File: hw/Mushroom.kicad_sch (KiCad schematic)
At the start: 4 parts, among them U1 STM32G030F6Px, U2 LPS22HH, U3 SHT30-DIS, U4 BH1750FVI-TR

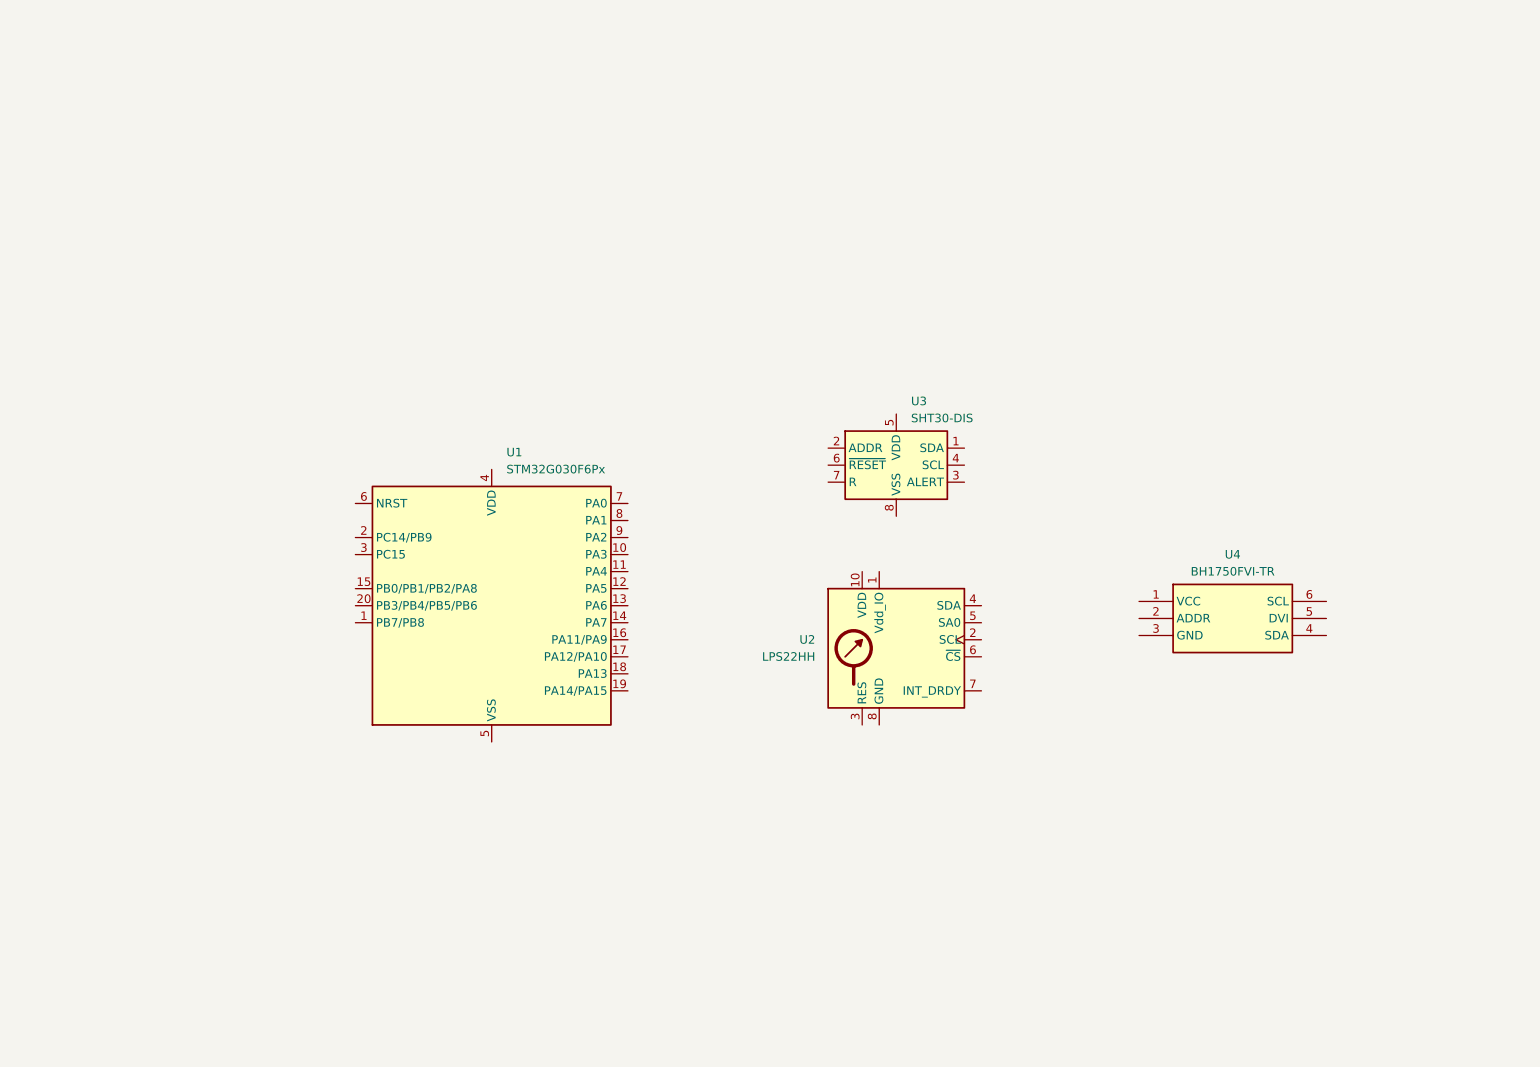
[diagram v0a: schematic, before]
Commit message: Finish schematic
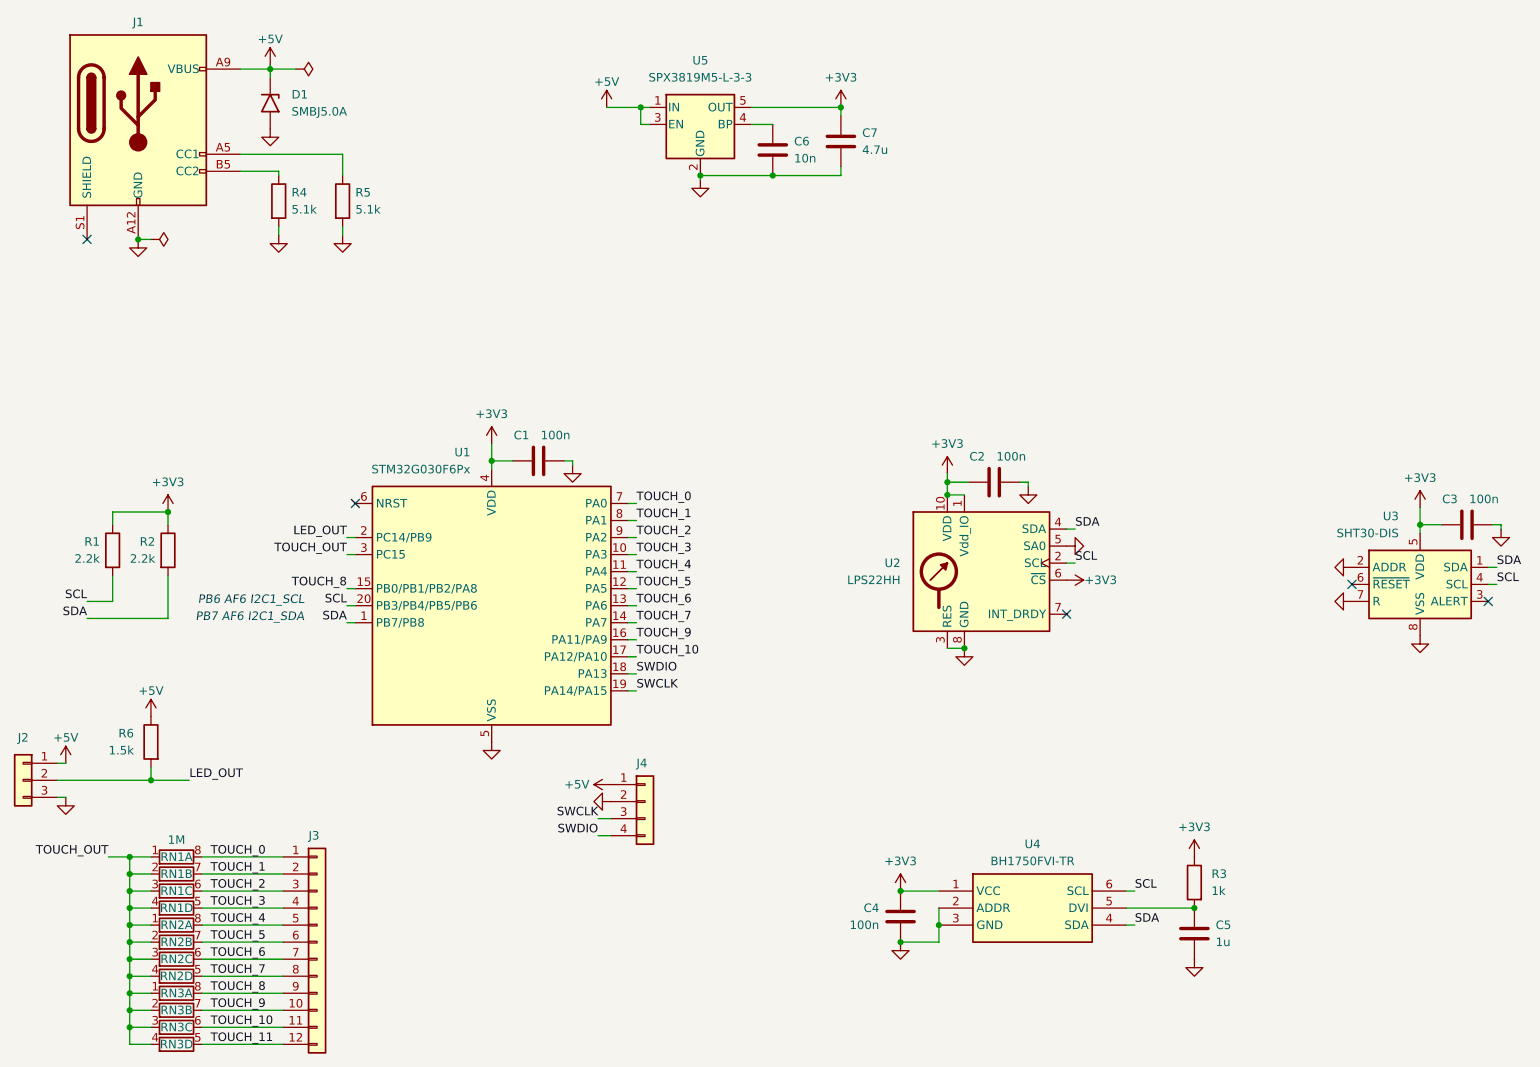
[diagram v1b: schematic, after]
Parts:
- added C1, C2, C3, C4: 100n, Capacitor_SMD:C_0402_1005Metric, symbol Device:C
- added C5: 1u, Capacitor_SMD:C_0402_1005Metric, symbol Device:C
- added C6: 10n, Capacitor_SMD:C_0402_1005Metric, symbol Device:C
- added C7: 4.7u, Capacitor_SMD:C_0402_1005Metric, symbol Device:C
- added D1: SMBJ5.0A, Diode_SMD:D_SMB, symbol Diode:SMF5V0A
- added J1: USB_C_Receptacle_PowerOnly_6P, Mushroom_footprints:USB_C_Receptacle, symbol Connector:USB_C_Receptacle_PowerOnly_6P
- added J2: Conn_01x03, Connector_PinHeader_2.54mm:PinHeader_1x03_P2.54mm_Vertical, symbol Connector_Generic:Conn_01x03
- added J3: Conn_01x12, Connector_PinHeader_2.54mm:PinHeader_2x06_P2.54mm_Vertical, symbol Connector_Generic:Conn_01x12
- added J4: Conn_01x04, Mushroom_footprints:TestPoints_1x04_P2.0, symbol Connector_Generic:Conn_01x04
- added R1, R2: 2.2k, Resistor_SMD:R_0402_1005Metric, symbol Device:R
- added R3: 1k, Resistor_SMD:R_0402_1005Metric, symbol Device:R
- added R4, R5: 5.1k, Resistor_SMD:R_0402_1005Metric, symbol Device:R
- added R6: 1.5k, Resistor_SMD:R_0402_1005Metric, symbol Device:R
- added RN1, RN2, RN3: 1M, Resistor_SMD:R_Array_Convex_4x0402, symbol Mushroom_symbols:R_Network04_Split
- added U5: SPX3819M5-L-3-3, Package_TO_SOT_SMD:SOT-23-5, symbol Regulator_Linear:SPX3819M5-L-3-3
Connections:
- net SDA: now reaches U3.1 (SDA)
- net SDA: now also U1.1 (PB7/PB8), U2.4 (SDA), U4.4 (SDA), R2.2
- net GND: now reaches U3.2 (ADDR)
- net GND: now also U1.5 (VSS), U2.3 (RES), U2.5 (SA0), U2.8 (GND), U2.9 (GND), U3.7 (R), U3.8 (VSS), U3.9 (VSS), U4.2 (ADDR), U4.3 (GND), C1.2, C2.2, C3.2, C4.2, C5.2, C6.2, C7.2, D1.2 (A2), J1.A12 (GND), J1.B12 (GND), J2.3 (Pin_3), J4.2 (Pin_2), R4.2, R5.2, U5.2 (GND)
- net SCL: now reaches U3.4 (SCL)
- net SCL: now also U1.20 (PB3/PB4/PB5/PB6), U2.2 (SCL), U4.6 (SCL), R1.2
- net +3V3: now reaches U3.5 (VDD)
- net +3V3: now also U1.4 (VDD), U2.1 (Vdd_IO), U2.10 (VDD), U2.6 (~{CS}), U4.1 (VCC), C1.1, C2.1, C3.1, C4.1, C7.1, R1.1, R2.1, R3.1, U5.5 (OUT)
- net TOUCH_3: now reaches U1.10 (PA3)
- net TOUCH_3: now also J3.4 (Pin_4), RN1.5 (R4.2)
- net TOUCH_4: now reaches U1.11 (PA4)
- net TOUCH_4: now also J3.5 (Pin_5), RN2.8 (R1.2)
- net TOUCH_5: now reaches U1.12 (PA5)
- net TOUCH_5: now also J3.6 (Pin_6), RN2.7 (R2.2)
- net TOUCH_6: now reaches U1.13 (PA6)
- net TOUCH_6: now also J3.7 (Pin_7), RN2.6 (R3.2)
- net TOUCH_7: now reaches U1.14 (PA7)
- net TOUCH_7: now also J3.8 (Pin_8), RN2.5 (R4.2)
- net TOUCH_8: now reaches U1.15 (PB0/PB1/PB2/PA8)
- net TOUCH_8: now also J3.9 (Pin_9), RN3.8 (R1.2)
- net TOUCH_9: now reaches U1.16 (PA11/PA9)
- net TOUCH_9: now also J3.10 (Pin_10), RN3.7 (R2.2)
- net TOUCH_10: now reaches U1.17 (PA12/PA10)
- net TOUCH_10: now also J3.11 (Pin_11), RN3.6 (R3.2)
- net SWDIO: now reaches U1.18 (PA13)
- net SWDIO: now also J4.4 (Pin_4)
- net SWCLK: now reaches U1.19 (PA14/PA15)
- net SWCLK: now also J4.3 (Pin_3)
- net LED_OUT: now reaches U1.2 (PC14/PB9)
- net LED_OUT: now also J2.2 (Pin_2), R6.2
- net TOUCH_OUT: now reaches U1.3 (PC15)
- net TOUCH_OUT: now also RN1.1 (R1.1), RN1.2 (R2.1), RN1.3 (R3.1), RN1.4 (R4.1), RN2.1 (R1.1), RN2.2 (R2.1), RN2.3 (R3.1), RN2.4 (R4.1), RN3.1 (R1.1), RN3.2 (R2.1), RN3.3 (R3.1), RN3.4 (R4.1)
- net TOUCH_0: now reaches U1.7 (PA0)
- net TOUCH_0: now also J3.1 (Pin_1), RN1.8 (R1.2)
- net TOUCH_1: now reaches U1.8 (PA1)
- net TOUCH_1: now also J3.2 (Pin_2), RN1.7 (R2.2)
- net TOUCH_2: now reaches U1.9 (PA2)
- net TOUCH_2: now also J3.3 (Pin_3), RN1.6 (R3.2)
- net at U4.5 (DVI): now also C5.1, R3.2
- new net: C6.1, U5.4 (BP)
- new net: J1.A5 (CC1), R5.1
- new net: J1.B5 (CC2), R4.1
- new net +5V: D1.1 (A1), J1.A9 (VBUS), J1.B9 (VBUS), J2.1 (Pin_1), J4.1 (Pin_1), R6.1, U5.1 (IN), U5.3 (EN)
- new net TOUCH_11: J3.12 (Pin_12), RN3.5 (R4.2)
- no-connect marks 0 -> 5
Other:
- note added: "PB6 AF6 I2C1_SCL"
- note added: "PB7 AF6 I2C1_SDA"
- moved on the sheet: U2, U3, U4

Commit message: 🚧 Preliminary layout & routing
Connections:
- net TOUCH_11 is gone; now on net SWDIO: J3.12 (Pin_12), RN3.5 (R4.2)
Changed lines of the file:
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@@
     (stroke (width 0) (type default))
   )
-  (wire (pts (xy 41.91 82.55) (xy 40.64 82.55))
+  (wire (pts (xy 40.64 82.55) (xy 51.435 82.55))
     (stroke (width 0) (type default))
   )
@@
     (effects (font (size 1.27 1.27)) (justify left bottom))
   )
+  (label "TOUCH_11" (at 51.435 82.55 0) (fields_autoplaced)
+    (effects (font (size 1.27 1.27)) (justify left bottom))
+  )

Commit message: Finish board design
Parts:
- J3: footprint Connector_PinHeader_2.54mm:PinHeader_2x06_P2.54mm_Vertical -> Mushroom_footprints:Arc_Pins_12
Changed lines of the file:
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@@
       (effects (font (size 1.27 1.27)) (justify left) hide)
     )
-    (property "Footprint" "Connector_PinHeader_2.54mm:PinHeader_2x06_P2.54mm_Vertical" (at -5.715 122.555 0)
+    (property "Footprint" "Mushroom_footprints:Arc_Pins_12" (at -5.715 122.555 0)
       (effects (font (size 1.27 1.27)) hide)
     )

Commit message: 🎉 Submit for fab (Rev. 1)
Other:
- note added: "FT"
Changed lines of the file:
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@@
+    (effects (font (size 1.27 1.27) italic) (justify right bottom))
+  )
+  (text "FT" (at -12.065 62.23 0)
     (effects (font (size 1.27 1.27) italic) (justify right bottom))
   )

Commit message: Revise board schematic
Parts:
- removed J1: USB_C_Receptacle_PowerOnly_6P, Mushroom_footprints:USB_C_Receptacle, symbol Connector:USB_C_Receptacle_PowerOnly_6P
- removed RN2, RN3: 1M, Resistor_SMD:R_Array_Convex_4x0402, symbol Mushroom_symbols:R_Network04_Split
- added C10, C9: 100n, Capacitor_SMD:C_0402_1005Metric, symbol Device:C
- added C8: 1u, Capacitor_SMD:C_0402_1005Metric, symbol Device:C
- added J1: USB_C_Receptacle_USB2.0_14P, Connector_USB:USB_C_Receptacle_HRO_TYPE-C-31-M-12, symbol Connector:USB_C_Receptacle_USB2.0_14P
- added U6: CH343P, Package_DFN_QFN:QFN-16-1EP_3x3mm_P0.5mm_EP1.9x1.9mm, symbol Mushroom_symbols:CH343P
- J3: value Conn_01x12 -> Conn_01x04; symbol Connector_Generic:Conn_01x12 -> Connector_Generic:Conn_01x04
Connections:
- net +3V3: now also C10.1, U6.1 (VIO)
- net +5V: now also C8.1, J1.A4 (VBUS), J1.A9 (VBUS), J1.B4 (VBUS), J1.B9 (VBUS), U6.3 (VDD5), U6.9 (VBUS)
- net GND: now also C10.2, C8.2, C9.2, J1.A1 (GND), J1.A12 (GND), J1.B1 (GND), J1.B12 (GND), U6.17 (GND), U6.2 (GND)
- net SWDIO: no longer J3.12 (Pin_12)
- net TOUCH_0: now also U1.11 (PA4); no longer U1.7 (PA0)
- net TOUCH_1: now also U1.12 (PA5); no longer U1.8 (PA1)
- net TOUCH_2: now also U1.13 (PA6); no longer U1.9 (PA2)
- net TOUCH_3: now also U1.14 (PA7); no longer U1.10 (PA3)
- net TOUCH_OUT: now also U1.15 (PB0/PB1/PB2/PA8); no longer U1.3 (PC15)
- net CC1: now reaches R5.1
- net CC1: now also U1.16 (PA11/PA9), J1.A5 (CC1)
- net CC2: now reaches R4.1
- net CC2: now also U1.17 (PA12/PA10), J1.B5 (CC2)
- removed net TOUCH_10: J3.11 (Pin_11), U1.17 (PA12/PA10)
- removed net TOUCH_4: J3.5 (Pin_5), U1.11 (PA4)
- removed net TOUCH_5: J3.6 (Pin_6), U1.12 (PA5)
- removed net TOUCH_6: J3.7 (Pin_7), U1.13 (PA6)
- removed net TOUCH_7: J3.8 (Pin_8), U1.14 (PA7)
- removed net TOUCH_8: J3.9 (Pin_9), U1.15 (PB0/PB1/PB2/PA8)
- removed net TOUCH_9: J3.10 (Pin_10), U1.16 (PA11/PA9)
- new net: C9.1, U6.6 (V3)
- new net UART_RX: U1.10 (PA3), U6.5 (RXD)
- new net UART_TX: U1.9 (PA2), U6.4 (TXD)
- new net USB_D+: J1.A6 (D+), J1.B6 (D+), U6.7 (UD+)
- new net USB_D-: J1.A7 (D-), J1.B7 (D-), U6.8 (UD-)
- no-connect marks 5 -> 15
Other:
- note added: "ADC_IN15"
- note added: "ADC_IN16"
- note added: "PA2 AF1 USART2_TX"
- note added: "PA3 AF1 USART2_RX"
- moved on the sheet: D1, R4, R5

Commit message: Preliminary layout & routing
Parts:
- J3: footprint Mushroom_footprints:Arc_Pins_12 -> Mushroom_footprints:Arc_Pins_04
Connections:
- net +3V3: now also C8.1, U6.3 (VDD5)
- net +5V: no longer C8.1, U6.3 (VDD5)
- net CC1: now also U1.8 (PA1); no longer U1.16 (PA11/PA9)
- net CC2: now also U1.11 (PA4); no longer U1.17 (PA12/PA10)
- net LED_OUT: now also U1.12 (PA5); no longer U1.2 (PC14/PB9)
- net TOUCH_0: now also U1.14 (PA7); no longer U1.11 (PA4)
- net TOUCH_1: now also U1.15 (PB0/PB1/PB2/PA8); no longer U1.12 (PA5)
- net TOUCH_2: now also U1.16 (PA11/PA9); no longer U1.13 (PA6)
- net TOUCH_3: now also U1.17 (PA12/PA10); no longer U1.14 (PA7)
- net TOUCH_OUT: now also U1.13 (PA6); no longer U1.15 (PB0/PB1/PB2/PA8)

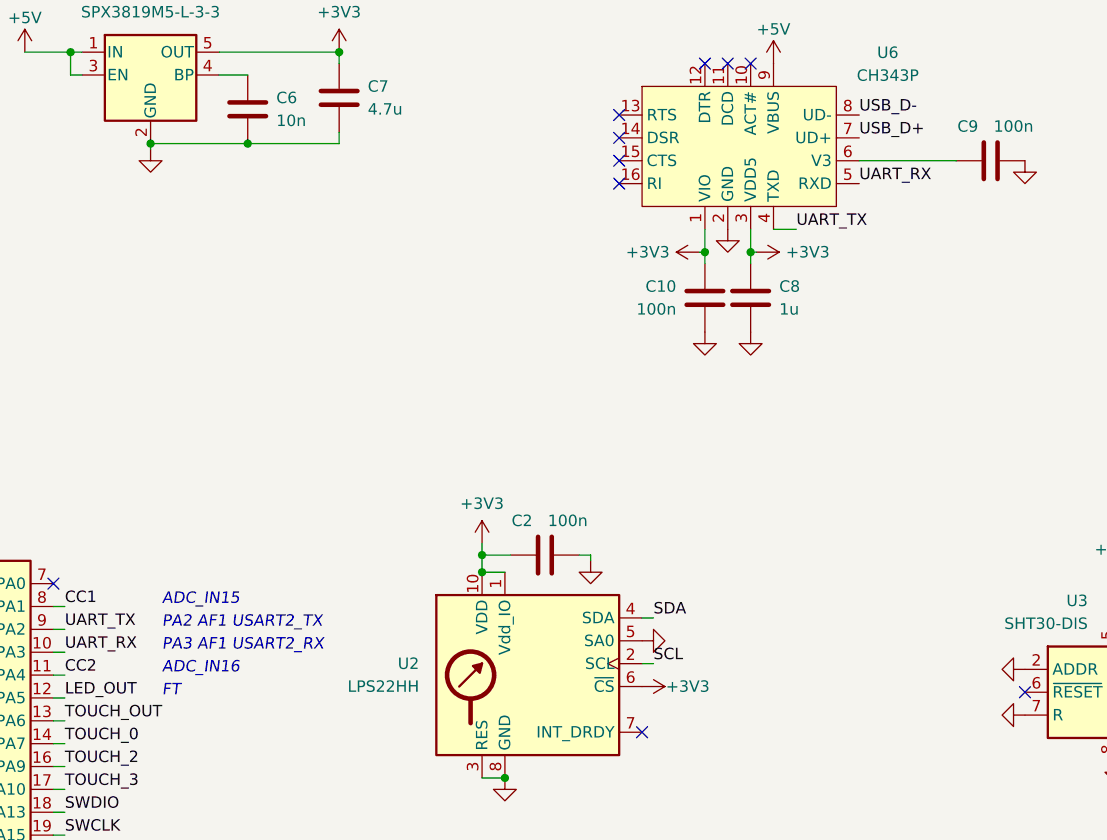
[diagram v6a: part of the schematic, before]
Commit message: Fix TX/RX lines; re-submit for fab (Rev. 2)
Previous order was cancelled (Y52, Y53)
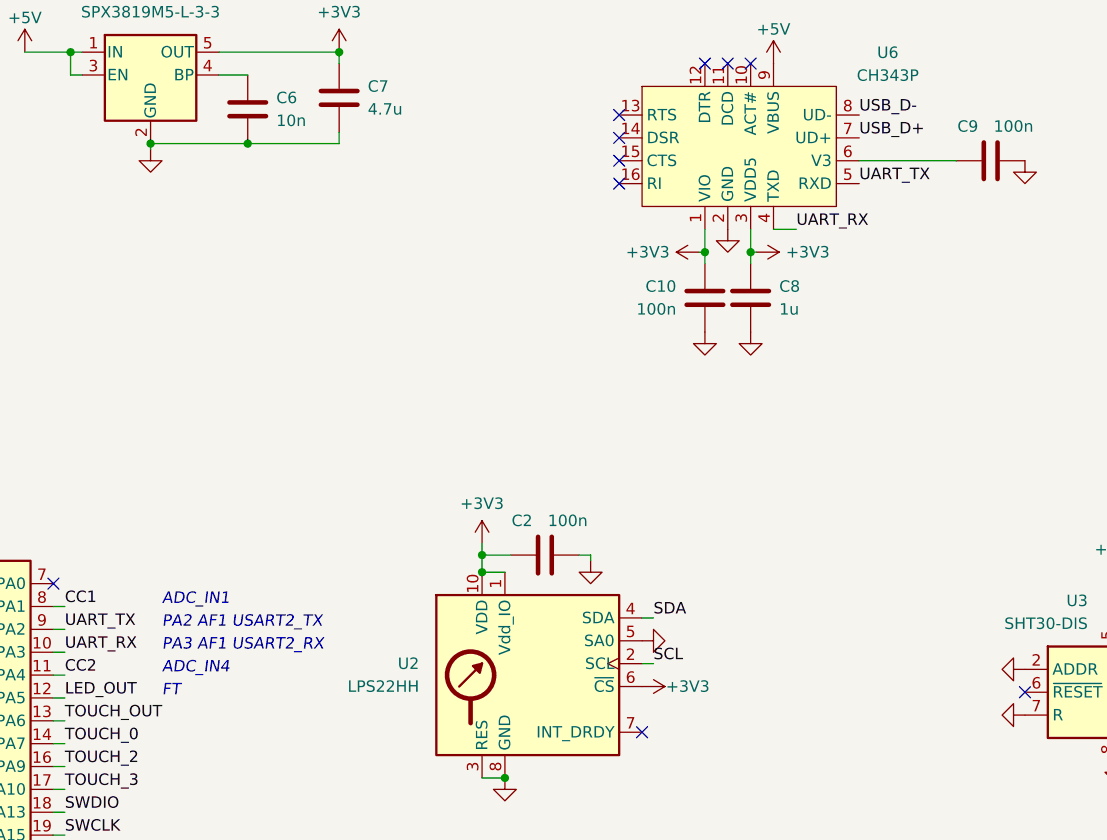
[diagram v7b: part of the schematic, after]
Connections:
- net UART_RX: now also U6.4 (TXD); no longer U6.5 (RXD)
- net UART_TX: now also U6.5 (RXD); no longer U6.4 (TXD)
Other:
- note added: "ADC_IN1"
- note added: "ADC_IN4"
- note removed: "ADC_IN15"
- note removed: "ADC_IN16"
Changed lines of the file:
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@@
     (effects (font (size 1.27 1.27) italic) (justify left bottom))
   )
-  (text "ADC_IN15" (at 52.705 59.69 0)
+  (text "ADC_IN1" (at 52.705 59.69 0)
     (effects (font (size 1.27 1.27) italic) (justify left bottom))
   )
@@
     (effects (font (size 1.27 1.27) italic) (justify left bottom))
   )
-  (text "ADC_IN16" (at 52.705 67.31 0)
+  (text "ADC_IN4" (at 52.705 67.31 0)
     (effects (font (size 1.27 1.27) italic) (justify left bottom))
   )
@@
     (effects (font (size 1.27 1.27)) (justify left bottom))
   )
-  (label "UART_RX" (at 130.175 12.7 0) (fields_autoplaced)
+  (label "UART_TX" (at 130.175 12.7 0) (fields_autoplaced)
     (effects (font (size 1.27 1.27)) (justify left bottom))
   )
@@
     (effects (font (size 1.27 1.27)) (justify left bottom))
   )
-  (label "UART_TX" (at 123.19 17.78 0) (fields_autoplaced)
+  (label "UART_RX" (at 123.19 17.78 0) (fields_autoplaced)
     (effects (font (size 1.27 1.27)) (justify left bottom))
   )
